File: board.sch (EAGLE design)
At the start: 14 parts, among them J1 5.5x2.1mm Barrel, T1 TIP122

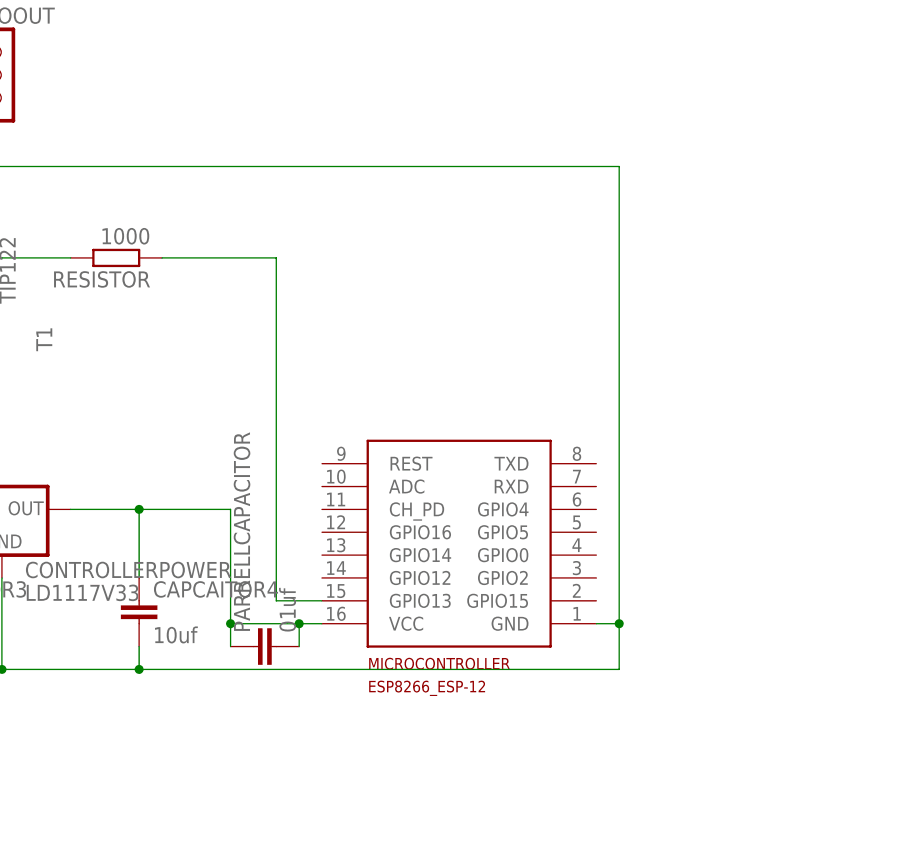
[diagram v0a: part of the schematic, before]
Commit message: Change base board to esp 01
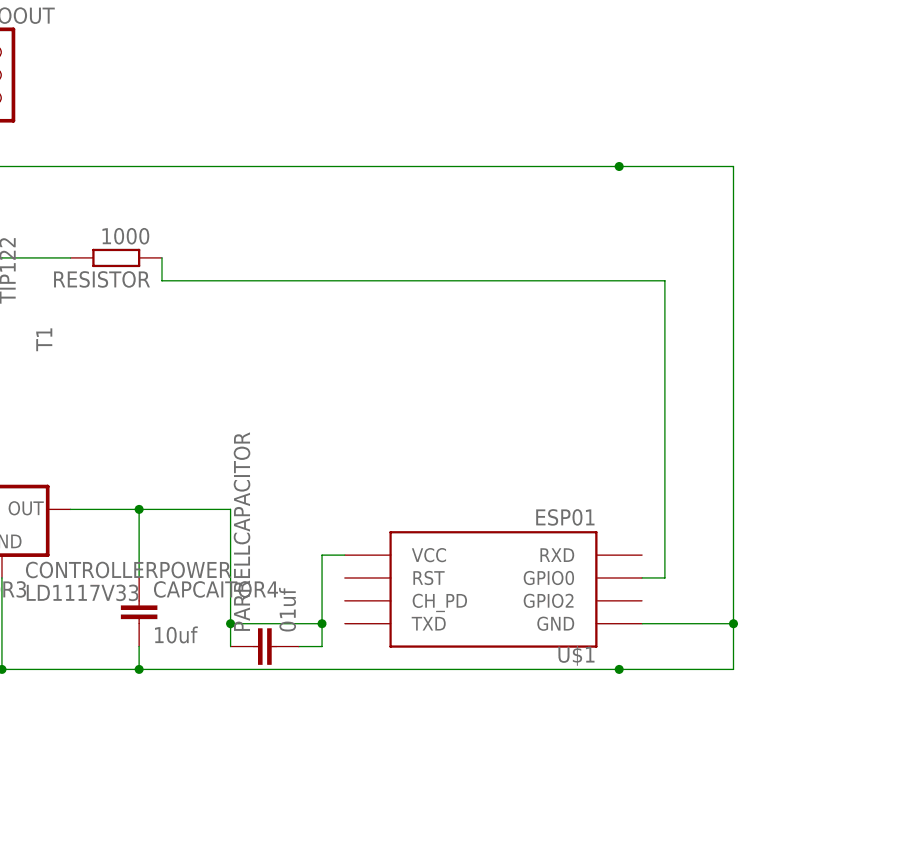
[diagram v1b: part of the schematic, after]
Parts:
- removed MICROCONTROLLER: ESP8266_ESP-12, ESP8266-ESP12:ESP8266_ESP-12
- added U$1: ESP01, esp8266modules:ESP01
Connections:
- net GND: now also U$1.GND; no longer MICROCONTROLLER.GND
- net N$7: now also U$1.VCC; no longer MICROCONTROLLER.VCC
- net N$9: now also U$1.GPIO0; no longer MICROCONTROLLER.GPIO13
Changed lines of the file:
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@@
 <part name="OUTPUTINDUCTOR" library="eagle-ltspice" library_urn="urn:adsk.eagle:library:217" deviceset="L" device="0204/7" package3d_urn="urn:adsk.eagle:package:13274/1" value="330uH"/>
 <part name="CAPCAITOR1" library="capacitor-wima" library_urn="urn:adsk.eagle:library:116" deviceset="C" device="5/2.5" package3d_urn="urn:adsk.eagle:package:5426/1" value="1000uf"/>
-<part name="MICROCONTROLLER" library="ESP8266-ESP12" deviceset="ESP8266_ESP-12" device=""/>
 <part name="CONTROLLERPOWER" library="LD1117V33" deviceset="LD1117V33" device=""/>
 <part name="CAPCAITOR3" library="capacitor-wima" library_urn="urn:adsk.eagle:library:116" deviceset="C" device="5/2.5" package3d_urn="urn:adsk.eagle:package:5426/1" value="100nf"/>
@@
 <part name="D1" library="_mod_diode" deviceset="1N581*" device="" technology="7-T"/>
 <part name="PARRELLCAPACITOR" library="capacitor-wima" library_urn="urn:adsk.eagle:library:116" deviceset="C" device="5/2.5" package3d_urn="urn:adsk.eagle:package:5426/1" value="01uf"/>
+<part name="U$1" library="esp8266modules" deviceset="ESP01" device=""/>
 </parts>
 <sheets>
@@
 <attribute name="VALUE" x="-8.636" y="41.021" size="1.778" layer="96"/>
 </instance>
-<instance part="MICROCONTROLLER" gate="G$1" x="76.2" y="53.34" smashed="yes">
-<attribute name="NAME" x="58.42" y="38.1" size="1.27" layer="94"/>
-</instance>
 <instance part="CONTROLLERPOWER" gate="G$1" x="17.78" y="53.34" smashed="yes">
 <attribute name="NAME" x="20.32" y="48.26" size="1.778" layer="95"/>
@@
 <attribute name="NAME" x="45.339" y="42.164" size="1.778" layer="95" rot="R90"/>
 <attribute name="VALUE" x="50.419" y="42.164" size="1.778" layer="96" rot="R90"/>
+</instance>
+<instance part="U$1" gate="G$1" x="71.12" y="50.8" smashed="yes" rot="R180">
+<attribute name="NAME" x="83.82" y="40.64" size="1.778" layer="95" rot="R180"/>
+<attribute name="VALUE" x="83.82" y="55.88" size="1.778" layer="95" rot="R180"/>
 </instance>
 </instances>
@@
 <wire x1="33.02" y1="38.1" x2="17.78" y2="38.1" width="0.1524" layer="91"/>
 <junction x="33.02" y="38.1"/>
-<pinref part="MICROCONTROLLER" gate="G$1" pin="GND"/>
-<wire x1="83.82" y1="43.18" x2="86.36" y2="43.18" width="0.1524" layer="91"/>
-<wire x1="86.36" y1="43.18" x2="86.36" y2="38.1" width="0.1524" layer="91"/>
 <wire x1="86.36" y1="38.1" x2="33.02" y2="38.1" width="0.1524" layer="91"/>
 <pinref part="SERVOOUT" gate="A" pin="1"/>
@@
 <wire x1="-91.44" y1="50.8" x2="-88.9" y2="50.8" width="0.1524" layer="91"/>
 <wire x1="-88.9" y1="50.8" x2="-88.9" y2="38.1" width="0.1524" layer="91"/>
-<junction x="86.36" y="43.18"/>
-<pinref part="T1" gate="G$1" pin="E"/>
-<wire x1="10.16" y1="91.44" x2="10.16" y2="93.98" width="0.1524" layer="91"/>
-<wire x1="10.16" y1="93.98" x2="86.36" y2="93.98" width="0.1524" layer="91"/>
-<wire x1="86.36" y1="93.98" x2="86.36" y2="43.18" width="0.1524" layer="91"/>
 <junction x="-33.02" y="38.1"/>
 <pinref part="D1" gate="G$1" pin="A"/>
 <wire x1="-33.02" y1="43.18" x2="-33.02" y2="38.1" width="0.1524" layer="91"/>
+<junction x="86.36" y="38.1"/>
+<wire x1="86.36" y1="38.1" x2="99.06" y2="38.1" width="0.1524" layer="91"/>
+<wire x1="10.16" y1="93.98" x2="86.36" y2="93.98" width="0.1524" layer="91"/>
+<pinref part="T1" gate="G$1" pin="E"/>
+<wire x1="10.16" y1="91.44" x2="10.16" y2="93.98" width="0.1524" layer="91"/>
+<junction x="86.36" y="93.98"/>
+<wire x1="86.36" y1="93.98" x2="99.06" y2="93.98" width="0.1524" layer="91"/>
+<wire x1="99.06" y1="93.98" x2="99.06" y2="43.18" width="0.1524" layer="91"/>
+<pinref part="U$1" gate="G$1" pin="GND"/>
+<wire x1="99.06" y1="43.18" x2="88.9" y2="43.18" width="0.1524" layer="91"/>
+<junction x="99.06" y="43.18"/>
+<wire x1="99.06" y1="38.1" x2="99.06" y2="43.18" width="0.1524" layer="91"/>
 </segment>
 </net>
@@
 <wire x1="33.02" y1="55.88" x2="33.02" y2="48.26" width="0.1524" layer="91"/>
 <junction x="33.02" y="55.88"/>
-<pinref part="MICROCONTROLLER" gate="G$1" pin="VCC"/>
-<wire x1="53.34" y1="43.18" x2="50.8" y2="43.18" width="0.1524" layer="91"/>
-<wire x1="50.8" y1="43.18" x2="43.18" y2="43.18" width="0.1524" layer="91"/>
+<wire x1="43.18" y1="40.64" x2="43.18" y2="43.18" width="0.1524" layer="91"/>
 <wire x1="43.18" y1="43.18" x2="43.18" y2="55.88" width="0.1524" layer="91"/>
 <wire x1="43.18" y1="55.88" x2="33.02" y2="55.88" width="0.1524" layer="91"/>
-<junction x="50.8" y="43.18"/>
+<pinref part="PARRELLCAPACITOR" gate="G$1" pin="1"/>
+<wire x1="43.18" y1="43.18" x2="53.34" y2="43.18" width="0.1524" layer="91"/>
+<wire x1="53.34" y1="43.18" x2="53.34" y2="50.8" width="0.1524" layer="91"/>
 <junction x="43.18" y="43.18"/>
-<pinref part="PARRELLCAPACITOR" gate="G$1" pin="1"/>
-<wire x1="43.18" y1="40.64" x2="43.18" y2="43.18" width="0.1524" layer="91"/>
+<pinref part="U$1" gate="G$1" pin="VCC"/>
+<wire x1="53.34" y1="50.8" x2="55.88" y2="50.8" width="0.1524" layer="91"/>
+<junction x="53.34" y="43.18"/>
 <pinref part="PARRELLCAPACITOR" gate="G$1" pin="2"/>
-<wire x1="50.8" y1="40.64" x2="50.8" y2="43.18" width="0.1524" layer="91"/>
+<wire x1="53.34" y1="43.18" x2="53.34" y2="40.64" width="0.1524" layer="91"/>
+<wire x1="53.34" y1="40.64" x2="50.8" y2="40.64" width="0.1524" layer="91"/>
 </segment>
 </net>
@@
 <pinref part="T1" gate="G$1" pin="B"/>
 <wire x1="25.4" y1="83.82" x2="17.78" y2="83.82" width="0.1524" layer="91"/>
-</segment>
-</net>
-<net name="N$9" class="0">
-<segment>
-<pinref part="RESISTOR" gate="G$1" pin="1"/>
-<wire x1="35.56" y1="83.82" x2="48.26" y2="83.82" width="0.1524" layer="91"/>
-<wire x1="48.26" y1="83.82" x2="48.26" y2="45.72" width="0.1524" layer="91"/>
-<pinref part="MICROCONTROLLER" gate="G$1" pin="GPIO13"/>
-<wire x1="48.26" y1="45.72" x2="53.34" y2="45.72" width="0.1524" layer="91"/>
 </segment>
 </net>
@@
 </segment>
 </net>
+<net name="N$9" class="0">
+<segment>
+<pinref part="RESISTOR" gate="G$1" pin="1"/>
+<wire x1="35.56" y1="83.82" x2="35.56" y2="81.28" width="0.1524" layer="91"/>
+<wire x1="35.56" y1="81.28" x2="91.44" y2="81.28" width="0.1524" layer="91"/>
+<wire x1="91.44" y1="81.28" x2="91.44" y2="48.26" width="0.1524" layer="91"/>
+<pinref part="U$1" gate="G$1" pin="GPIO0"/>
+<wire x1="91.44" y1="48.26" x2="88.9" y2="48.26" width="0.1524" layer="91"/>
+</segment>
+</net>

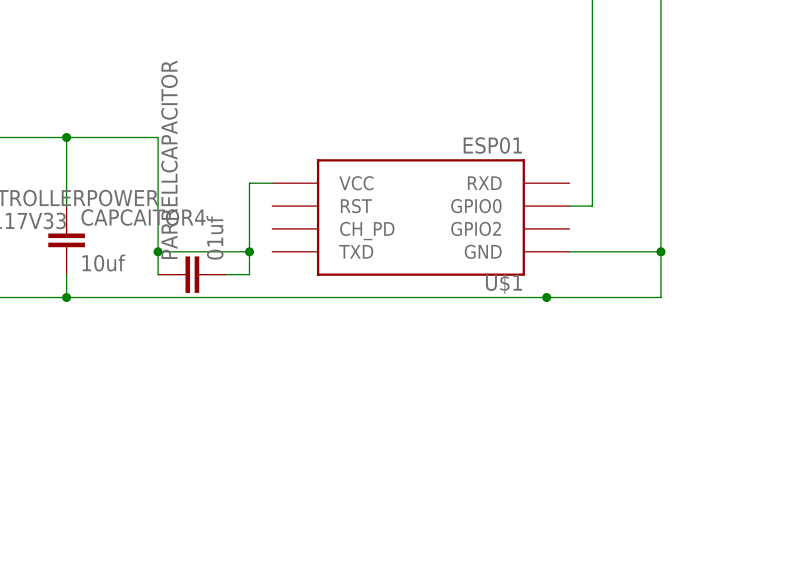
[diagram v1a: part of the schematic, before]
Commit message: Board update and autocad update to add nx files
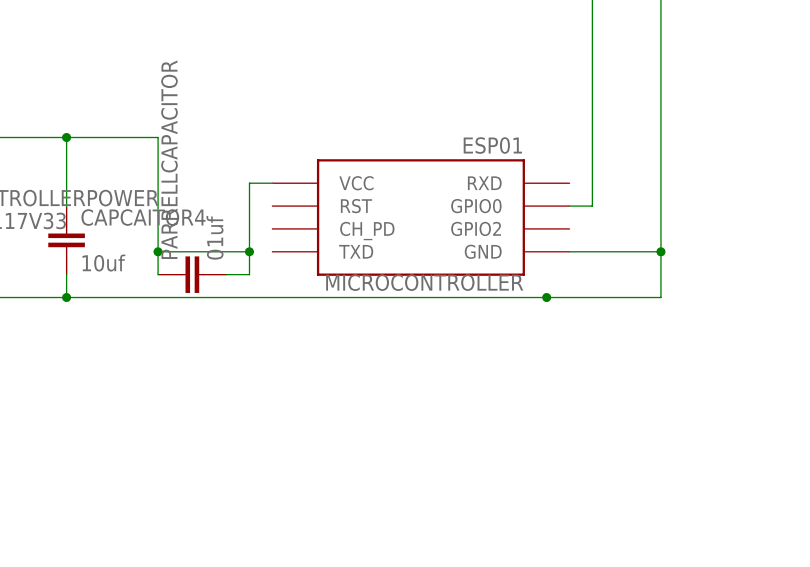
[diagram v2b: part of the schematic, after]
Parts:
- renumbered U$1 to MICROCONTROLLER
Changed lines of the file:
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@@
 <?xml version="1.0" encoding="utf-8"?>
 <!DOCTYPE eagle SYSTEM "eagle.dtd">
-<eagle version="9.2.2">
+<eagle version="9.2.0">
 <drawing>
 <settings>
@@
 <part name="D1" library="_mod_diode" deviceset="1N581*" device="" technology="7-T"/>
 <part name="PARRELLCAPACITOR" library="capacitor-wima" library_urn="urn:adsk.eagle:library:116" deviceset="C" device="5/2.5" package3d_urn="urn:adsk.eagle:package:5426/1" value="01uf"/>
-<part name="U$1" library="esp8266modules" deviceset="ESP01" device=""/>
+<part name="MICROCONTROLLER" library="esp8266modules" deviceset="ESP01" device=""/>
 </parts>
 <sheets>
@@
 </plain>
 <instances>
-<instance part="INPUTPOWER" gate="A" x="-58.42" y="55.88" smashed="yes">
+<instance part="INPUTPOWER" gate="A" x="-58.42" y="55.88">
 <attribute name="NAME" x="-66.04" y="64.16" size="1.778" layer="95"/>
 <attribute name="VALUE" x="-66.04" y="45.72" size="1.778" layer="96"/>
 </instance>
-<instance part="CAPCAITOR2" gate="G$1" x="-83.82" y="50.8" smashed="yes">
+<instance part="CAPCAITOR2" gate="G$1" x="-83.82" y="50.8">
 <attribute name="NAME" x="-82.296" y="51.181" size="1.778" layer="95"/>
 <attribute name="VALUE" x="-82.296" y="46.101" size="1.778" layer="96"/>
 </instance>
-<instance part="OUTPUTINDUCTOR" gate="G$1" x="-20.32" y="55.88" smashed="yes" rot="R90">
+<instance part="OUTPUTINDUCTOR" gate="G$1" x="-20.32" y="55.88" rot="R90">
 <attribute name="NAME" x="-16.51" y="54.3814" size="1.778" layer="95" rot="R180"/>
 <attribute name="VALUE" x="-16.51" y="59.182" size="1.778" layer="96" rot="R180"/>
 </instance>
-<instance part="CAPCAITOR1" gate="G$1" x="-10.16" y="45.72" smashed="yes">
+<instance part="CAPCAITOR1" gate="G$1" x="-10.16" y="45.72">
 <attribute name="NAME" x="-8.636" y="46.101" size="1.778" layer="95"/>
 <attribute name="VALUE" x="-8.636" y="41.021" size="1.778" layer="96"/>
 </instance>
-<instance part="CONTROLLERPOWER" gate="G$1" x="17.78" y="53.34" smashed="yes">
+<instance part="CONTROLLERPOWER" gate="G$1" x="17.78" y="53.34">
 <attribute name="NAME" x="20.32" y="48.26" size="1.778" layer="95"/>
 <attribute name="VALUE" x="20.32" y="45.72" size="1.778" layer="96"/>
 </instance>
-<instance part="CAPCAITOR3" gate="G$1" x="5.08" y="45.72" smashed="yes">
+<instance part="CAPCAITOR3" gate="G$1" x="5.08" y="45.72">
 <attribute name="NAME" x="6.604" y="46.101" size="1.778" layer="95"/>
 <attribute name="VALUE" x="6.604" y="41.021" size="1.778" layer="96"/>
 </instance>
-<instance part="CAPCAITOR4" gate="G$1" x="33.02" y="45.72" smashed="yes">
+<instance part="CAPCAITOR4" gate="G$1" x="33.02" y="45.72">
 <attribute name="NAME" x="34.544" y="46.101" size="1.778" layer="95"/>
 <attribute name="VALUE" x="34.544" y="41.021" size="1.778" layer="96"/>
 </instance>
-<instance part="SERVOOUT" gate="A" x="17.78" y="104.14" smashed="yes">
+<instance part="SERVOOUT" gate="A" x="17.78" y="104.14">
 <attribute name="NAME" x="11.43" y="109.855" size="1.778" layer="95"/>
 <attribute name="VALUE" x="11.43" y="96.52" size="1.778" layer="96"/>
 </instance>
-<instance part="J1" gate="G$1" x="-93.98" y="45.72" smashed="yes">
+<instance part="J1" gate="G$1" x="-93.98" y="45.72">
 <attribute name="VALUE" x="-104.14" y="55.88" size="1.778" layer="96" font="vector"/>
 <attribute name="NAME" x="-104.14" y="45.72" size="1.778" layer="95" font="vector"/>
 </instance>
-<instance part="T1" gate="G$1" x="15.24" y="83.82" smashed="yes" rot="R180">
+<instance part="T1" gate="G$1" x="15.24" y="83.82" rot="R180">
 <attribute name="NAME" x="21.59" y="76.2" size="1.778" layer="95" rot="R270"/>
 <attribute name="VALUE" x="19.304" y="78.74" size="1.778" layer="96" rot="R90"/>
 </instance>
-<instance part="RESISTOR" gate="G$1" x="30.48" y="83.82" smashed="yes" rot="R180">
+<instance part="RESISTOR" gate="G$1" x="30.48" y="83.82" rot="R180">
 <attribute name="NAME" x="34.29" y="82.3214" size="1.778" layer="95" rot="R180"/>
 <attribute name="VALUE" x="34.29" y="87.122" size="1.778" layer="96" rot="R180"/>
 </instance>
-<instance part="D1" gate="G$1" x="-33.02" y="45.72" smashed="yes" rot="R90">
+<instance part="D1" gate="G$1" x="-33.02" y="45.72" rot="R90">
 <attribute name="NAME" x="-34.925" y="43.434" size="1.778" layer="95" rot="R90"/>
 <attribute name="VALUE" x="-29.591" y="43.434" size="1.778" layer="96" rot="R90"/>
 </instance>
-<instance part="PARRELLCAPACITOR" gate="G$1" x="45.72" y="40.64" smashed="yes" rot="R90">
+<instance part="PARRELLCAPACITOR" gate="G$1" x="45.72" y="40.64" rot="R90">
 <attribute name="NAME" x="45.339" y="42.164" size="1.778" layer="95" rot="R90"/>
 <attribute name="VALUE" x="50.419" y="42.164" size="1.778" layer="96" rot="R90"/>
 </instance>
-<instance part="U$1" gate="G$1" x="71.12" y="50.8" smashed="yes" rot="R180">
+<instance part="MICROCONTROLLER" gate="G$1" x="71.12" y="50.8" rot="R180">
 <attribute name="NAME" x="83.82" y="40.64" size="1.778" layer="95" rot="R180"/>
 <attribute name="VALUE" x="83.82" y="55.88" size="1.778" layer="95" rot="R180"/>
@@
 <wire x1="86.36" y1="93.98" x2="99.06" y2="93.98" width="0.1524" layer="91"/>
 <wire x1="99.06" y1="93.98" x2="99.06" y2="43.18" width="0.1524" layer="91"/>
-<pinref part="U$1" gate="G$1" pin="GND"/>
+<pinref part="MICROCONTROLLER" gate="G$1" pin="GND"/>
 <wire x1="99.06" y1="43.18" x2="88.9" y2="43.18" width="0.1524" layer="91"/>
 <junction x="99.06" y="43.18"/>
@@
 <wire x1="53.34" y1="43.18" x2="53.34" y2="50.8" width="0.1524" layer="91"/>
 <junction x="43.18" y="43.18"/>
-<pinref part="U$1" gate="G$1" pin="VCC"/>
+<pinref part="MICROCONTROLLER" gate="G$1" pin="VCC"/>
 <wire x1="53.34" y1="50.8" x2="55.88" y2="50.8" width="0.1524" layer="91"/>
 <junction x="53.34" y="43.18"/>
@@
 <wire x1="35.56" y1="81.28" x2="91.44" y2="81.28" width="0.1524" layer="91"/>
 <wire x1="91.44" y1="81.28" x2="91.44" y2="48.26" width="0.1524" layer="91"/>
-<pinref part="U$1" gate="G$1" pin="GPIO0"/>
+<pinref part="MICROCONTROLLER" gate="G$1" pin="GPIO0"/>
 <wire x1="91.44" y1="48.26" x2="88.9" y2="48.26" width="0.1524" layer="91"/>
 </segment>

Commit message: Updated PCB and Gerber Files
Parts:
- renumbered CAPCAITOR1 to 5REGCAP, CAPCAITOR2 to BATCAP, CAPCAITOR3 to 3REGCAP, CAPCAITOR4 to 3REGOUTCAP, CONTROLLERPOWER to 3VOLTREG, D1 to 5REGDIO, INPUTPOWER to 5VOLTREG, J1 to POWJACK, MICROCONTROLLER to MICROCONT, OUTPUTINDUCTOR to 5REGINDUC, PARRELLCAPACITOR to CONTCAP, RESISTOR to OUTREST, T1 to TRANOUT
